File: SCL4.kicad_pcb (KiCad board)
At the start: 2 copper layers, 150.5 x 233.3 mm, 38 parts, among them J1 spare1, J2 spare2, J3 Siemens_A1010-A263, J4 SP1, J5 SP2, J6 Conn_01x08, J7 5V out, U1 MC3487DX, U2 MC3487DX, U3 TRAM Size 2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

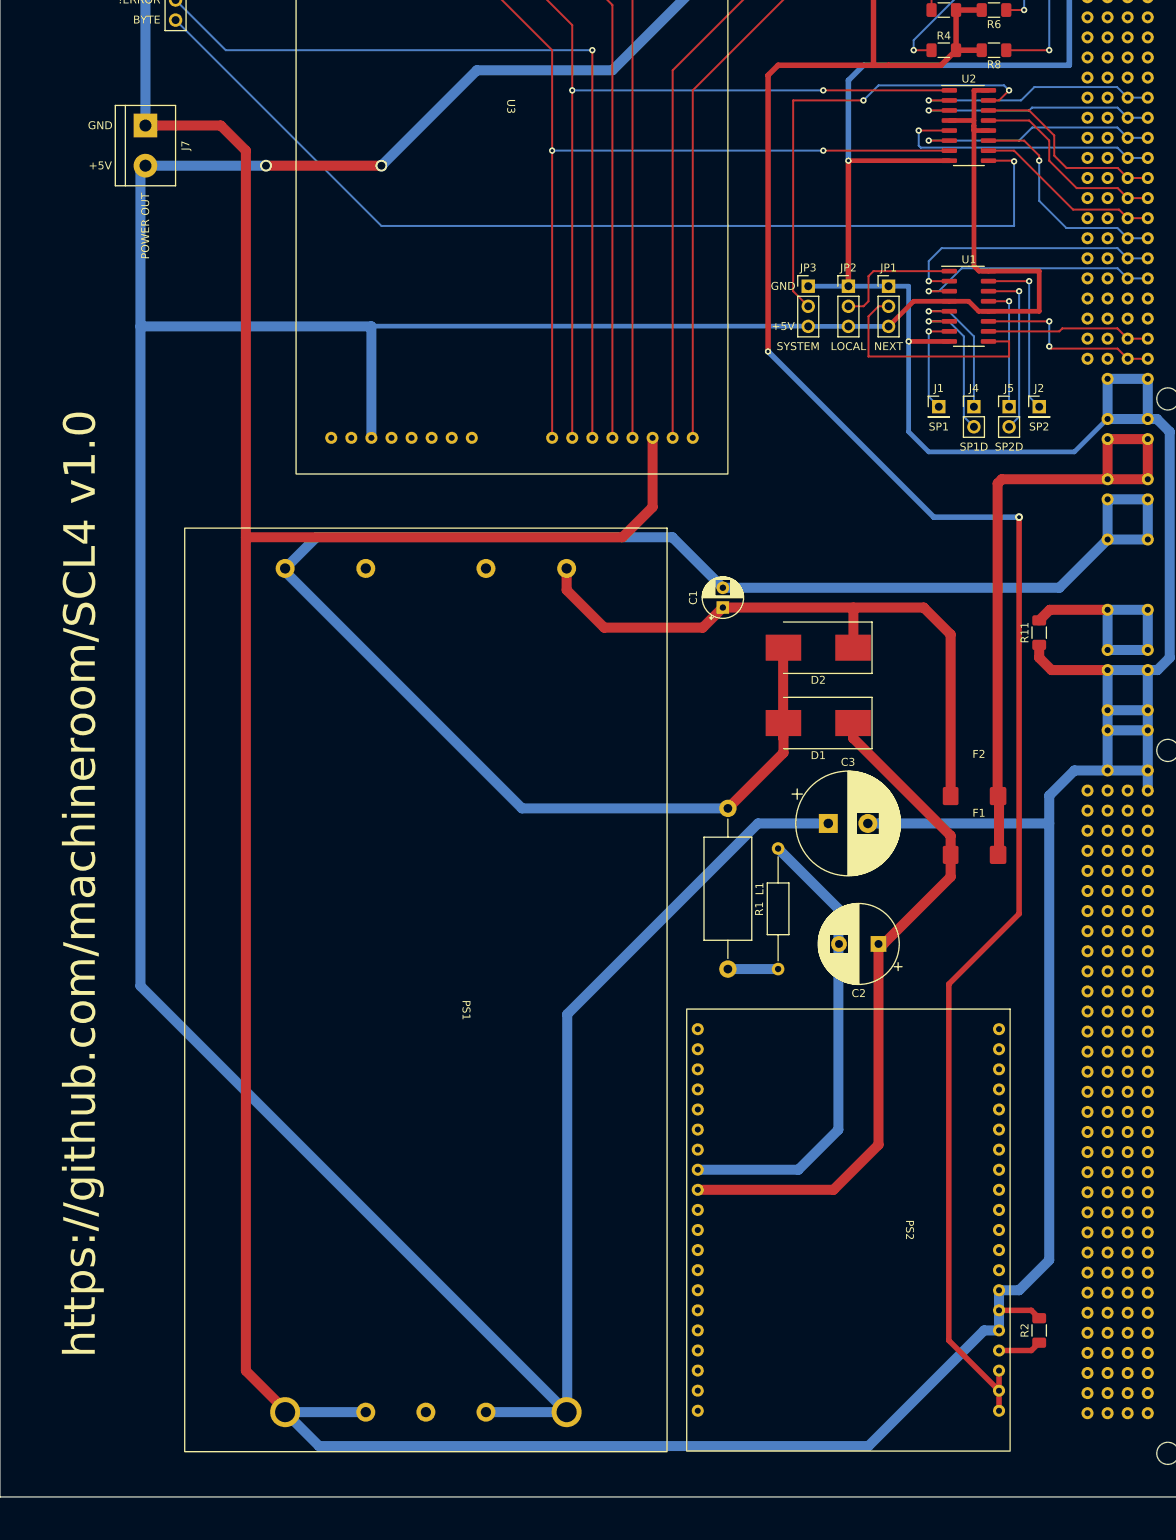
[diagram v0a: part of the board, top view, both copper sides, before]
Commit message: Add HLAA enable jumper
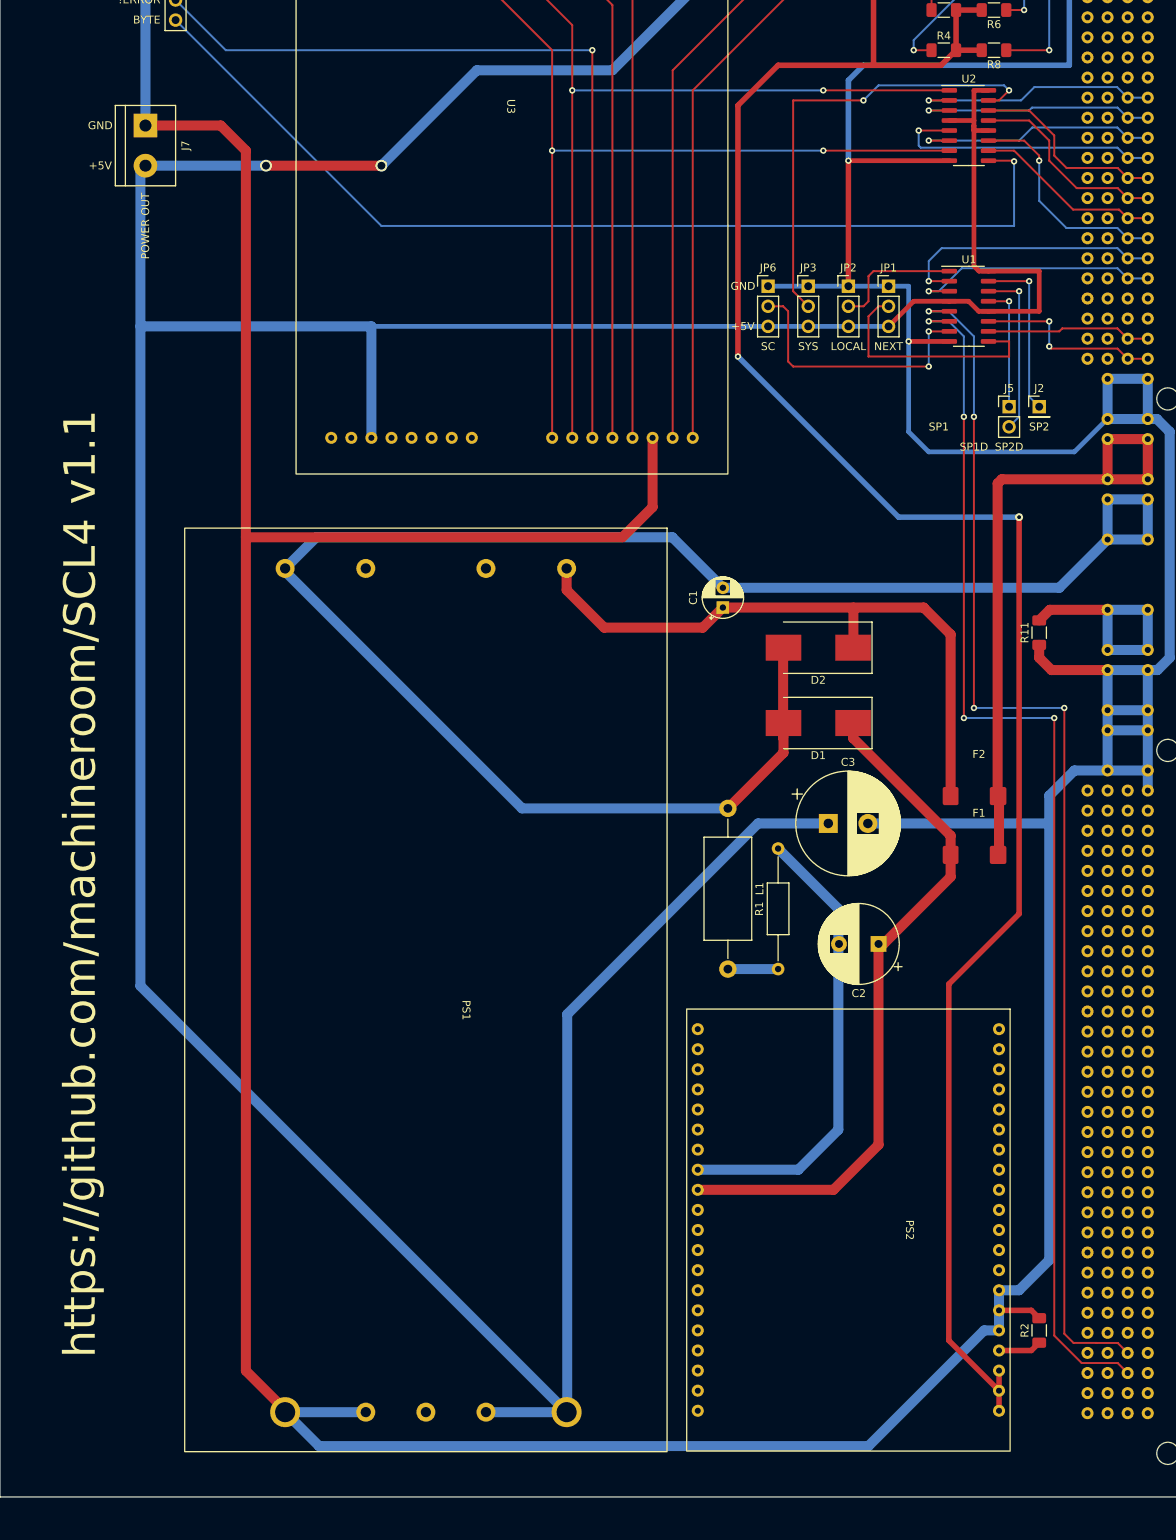
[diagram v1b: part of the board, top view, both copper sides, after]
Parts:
- removed J1: spare1, Connector_PinHeader_2.54mm:PinHeader_1x01_P2.54mm_Vertical
- removed J4: SP1, Connector_PinHeader_2.54mm:PinHeader_1x02_P2.54mm_Vertical
- added JP6: SC MODE, Connector_PinHeader_2.54mm:PinHeader_1x03_P2.54mm_Vertical, F.Cu at (251.5, 96.5)
- R4, R6, R7, R8: value 51R -> 510R
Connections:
- J3 pad B82: unconnected-(J3-PadB82) -> /HLAA_ENABLE
- J3 pad B83: unconnected-(J3-PadB83) -> //HLAA_ENABLE
- U1 pad 5: Net-(J4-Pad1) -> /HLAA_ENABLE
- U1 pad 6: Net-(J4-Pad2) -> //HLAA_ENABLE
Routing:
- net //HLAA_ENABLE: track 0.00 -> 156.9 mm, vias 0 -> 4
- net /HLAA_ENABLE: track 0.00 -> 156.2 mm, vias 0 -> 4
- net Net-(JP6-Pad2): track 12.7 -> 34.2 mm, vias 1 -> 2
- net Net-(J4-Pad2): track 19.8 -> 0.00 mm, vias 1 -> 0
- net Net-(J4-Pad1): track 18.5 -> 0.00 mm, vias 1 -> 0
- net -5V: track 296.2 -> 301.9 mm
- net GND: track 915.3 -> 920.3 mm
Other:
- board text added: "SC"
- board text added: "SYS"
- board text added: "https://github.com/machineroom/SCL4 v1.1"
- board text removed: "SYSTEM"
- board text removed: "https://github.com/machineroom/SCL4 v1.0"

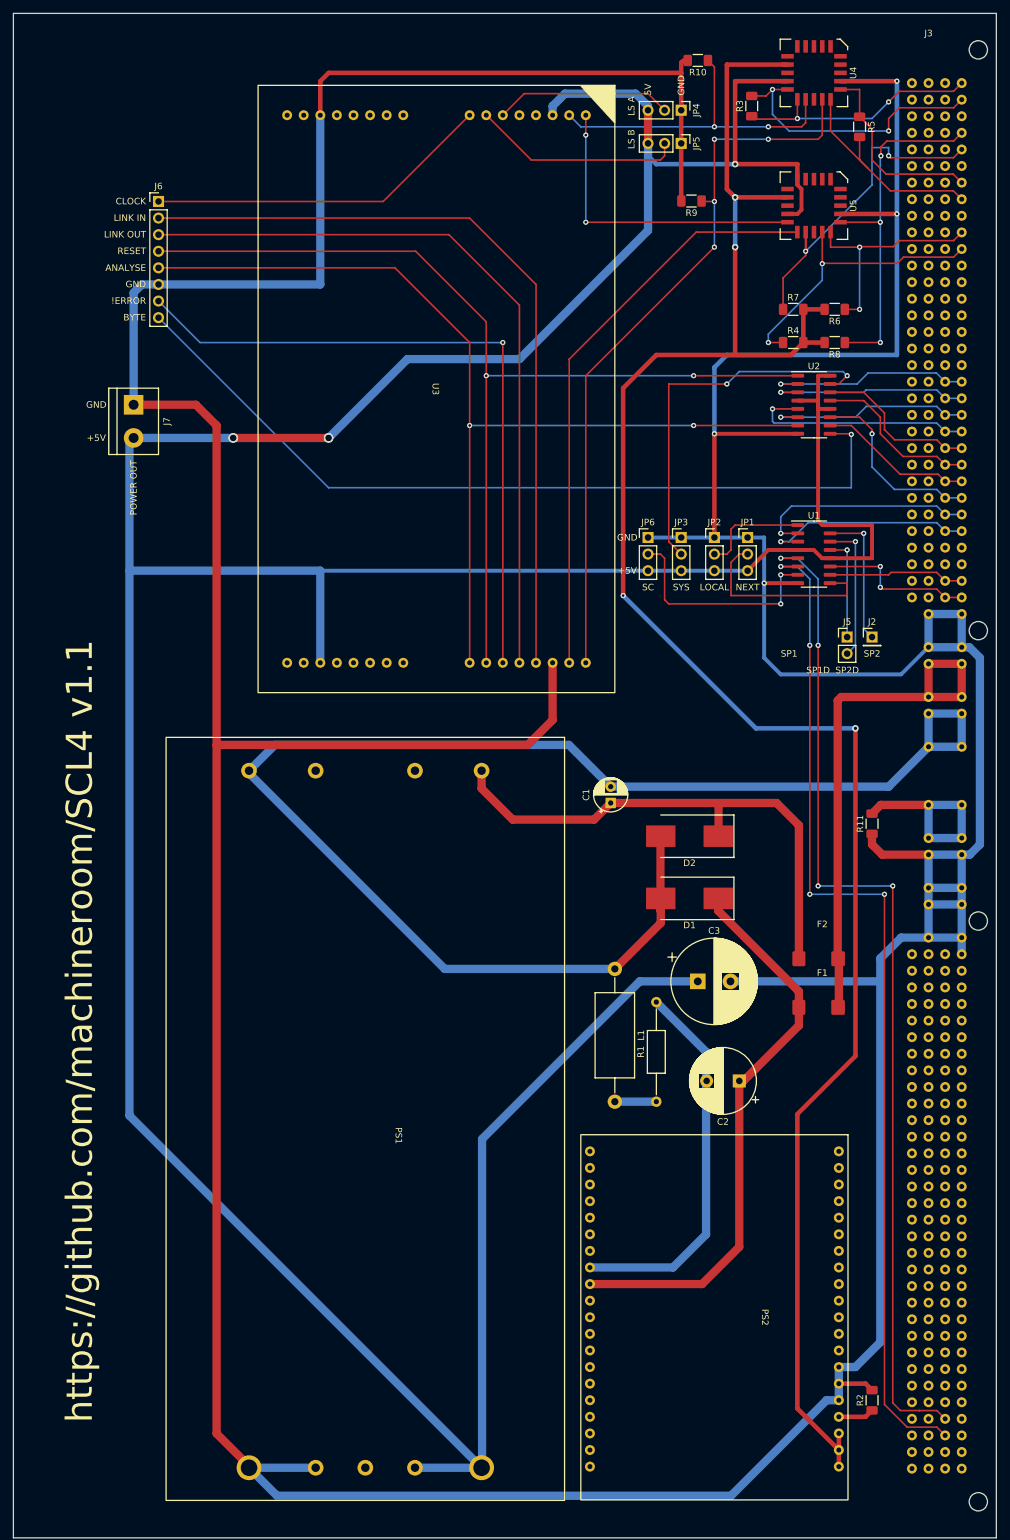
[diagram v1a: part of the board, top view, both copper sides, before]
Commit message: Major rework - fix -5V2 PSU orientation - analyse2 & reset2 signals for proc only operation (no HSL) - bring TRAM L1 and L3 to external header - lay down C3 to reduce height - decoupling - reduce + better match ECL trace lengths - remove R1 - reorder J6 to same as rpi interface header
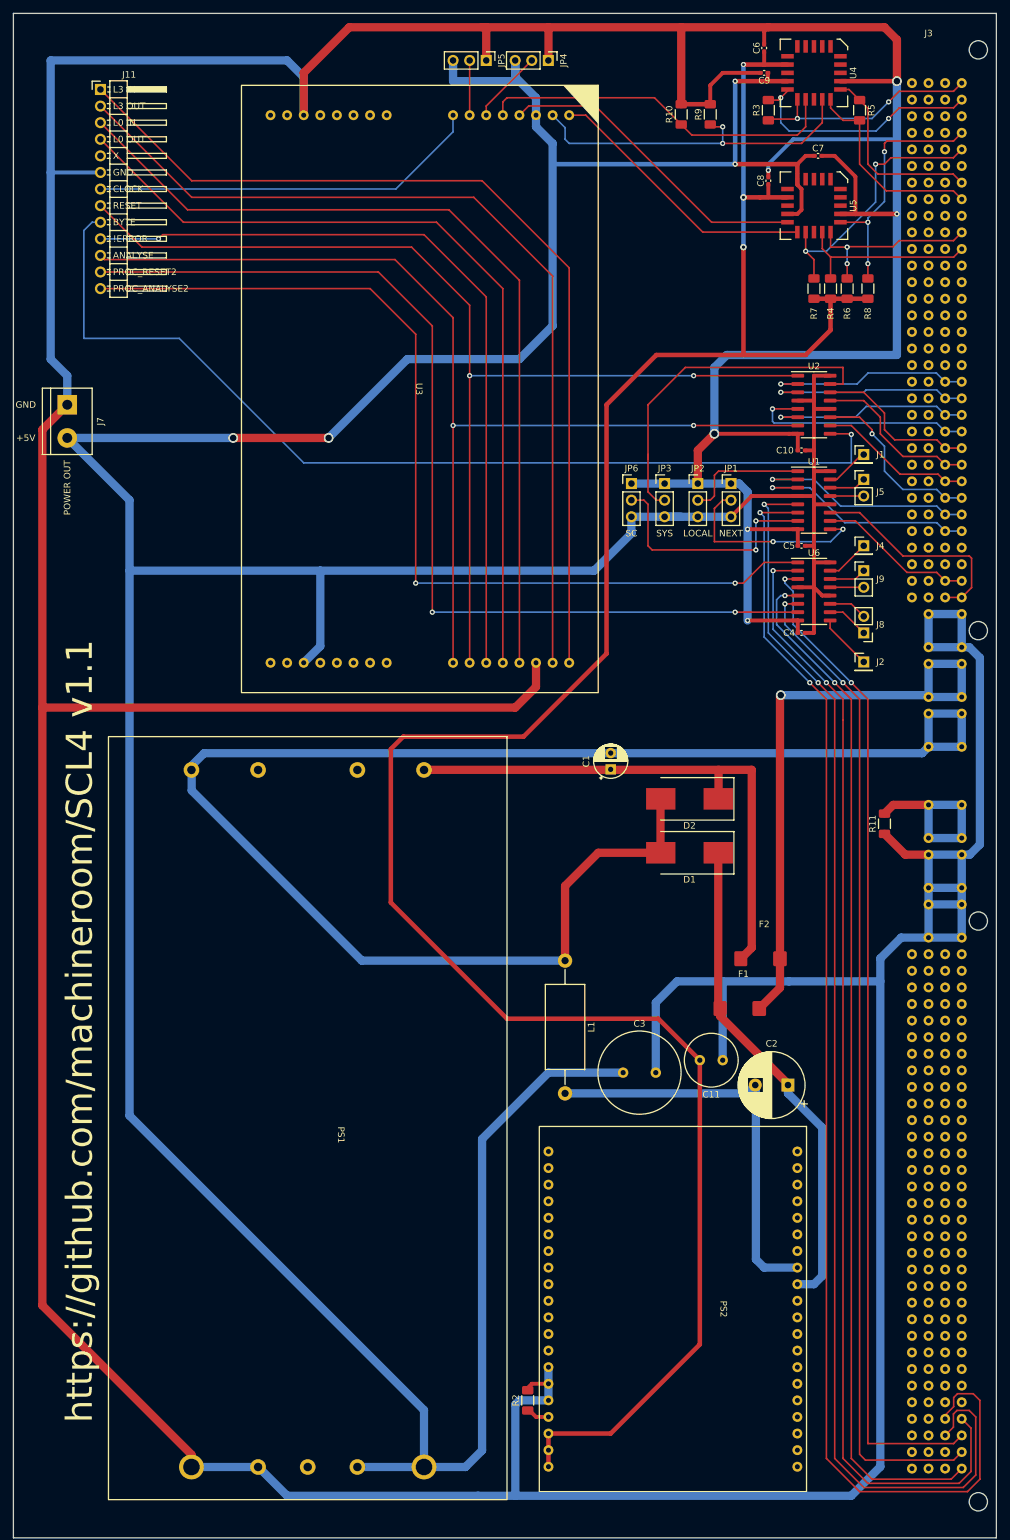
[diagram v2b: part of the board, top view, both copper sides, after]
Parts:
- removed J6: Conn_01x08, Connector_PinHeader_2.54mm:PinHeader_1x08_P2.54mm_Vertical
- removed R1: 10R 2%, Resistor_THT:R_Axial_DIN0207_L6.3mm_D2.5mm_P15.24mm_Horizontal
- added C10: 0.1uF, Capacitor_SMD:C_0402_1005Metric_Pad0.74x0.62mm_HandSolder, F.Cu at (275.0, 83.2)
- added C11: 220uF 63V, Capacitor_THT:C_Radial_D8.0mm_H11.5mm_P3.50mm, F.Cu at (262.9, 176.5)
- added C4: 0.1uF, Capacitor_SMD:C_0402_1005Metric_Pad0.74x0.62mm_HandSolder, F.Cu at (275.0, 111.1)
- added C5: 0.1uF, Capacitor_SMD:C_0402_1005Metric_Pad0.74x0.62mm_HandSolder, F.Cu at (275.0, 97.8)
- added C6: 0.1uF, Capacitor_SMD:C_0402_1005Metric_Pad0.74x0.62mm_HandSolder, F.Cu at (269.2, 21.6)
- added C7: 0.1uF, Capacitor_SMD:C_0402_1005Metric_Pad0.74x0.62mm_HandSolder, F.Cu at (277.5, 38.1)
- added C8: 0.1uF, Capacitor_SMD:C_0402_1005Metric_Pad0.74x0.62mm_HandSolder, F.Cu at (269.9, 41.9)
- added C9: 0.1uF, Capacitor_SMD:C_0402_1005Metric_Pad0.74x0.62mm_HandSolder, F.Cu at (269.2, 25.4)
- added J1: TSPARE1, Connector_PinHeader_2.54mm:PinHeader_1x01_P2.54mm_Vertical, F.Cu at (284.5, 83.8)
- added J11: Conn_01x10_Male, Connector_PinHeader_2.54mm:PinHeader_1x13_P2.54mm_Horizontal, F.Cu at (167.6, 27.9)
- added J4: TSPARE3, Connector_PinHeader_2.54mm:PinHeader_1x01_P2.54mm_Vertical, F.Cu at (284.5, 97.8)
- added J8: SPARE2, Connector_PinHeader_2.54mm:PinHeader_1x02_P2.54mm_Vertical, F.Cu at (284.5, 111.1)
- added J9: SPARE3, Connector_PinHeader_2.54mm:PinHeader_1x02_P2.54mm_Vertical, F.Cu at (284.5, 101.6)
- added U6: MC3487DX, Package_SO:SOIC-16_3.9x9.9mm_P1.27mm, F.Cu at (276.9, 104.8)
- C3: footprint Capacitor_THT:CP_Radial_D13.0mm_P5.00mm -> Capacitor_THT:C_Radial_D12.5mm_H20.0mm_P5.00mm
- J2: value spare2 -> TSPARE2
- J5: value SP2 -> SPARE1
- moved R2 52.7 mm to (233.0, 228.6)
- moved JP5 32.4 mm to (226.7, 23.5)
- moved J5 24.3 mm to (284.5, 87.6)
- moved JP4 21.7 mm to (236.2, 23.5)
- moved C3 18.1 mm to (247.7, 178.4)
- moved R9 13.6 mm to (261.0, 31.8), turned to 90 degrees
- moved F1 12.1 mm to (261.0, 166.4)
- moved J7 10.2 mm to (162.6, 76.2)
- moved R4 10.0 mm to (279.4, 58.4), turned to -90 degrees
- moved R8 9.69 mm to (285.1, 58.4), turned to -90 degrees
- moved F2 8.89 mm to (264.2, 158.8)
- moved PS1 8.82 mm to (229.9, 127.0)
- moved JP2 8.64 mm to (259.1, 88.3)
- moved JP3 8.64 mm to (254.0, 88.3)
- moved JP6 8.64 mm to (248.9, 88.3)
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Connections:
- net /SpeedA renamed Net-(JP4-Pad2)
- net /SpeedB renamed Net-(JP5-Pad2)
- J2 pad 1: Net-(J2-Pad1) -> /TSPARE2
- J3 pad A1: /L2IN -> /L1IN
- J3 pad A10: /L3OUT -> /L2OUT
- J3 pad A11: //L3OUT -> //L2OUT
- J3 pad A2: //L2IN -> //L1IN
- J3 pad A4: /L2OUT -> /L1OUT
- J3 pad A5: //L2OUT -> //L1OUT
- J3 pad A54: GND -> unconnected-(J3-PadA54)
- J3 pad A7: /L3IN -> /L2IN
- J3 pad A8: //L3IN -> //L2IN
- J3 pad A82: unconnected-(J3-PadA82) -> /PROC_ANALYSE2
- J3 pad A83: unconnected-(J3-PadA83) -> //PROC_ANALYSE2
- J3 pad A84: unconnected-(J3-PadA84) -> /PROC_RESET2
- J3 pad A85: unconnected-(J3-PadA85) -> //PROC_RESET2
- J5 pad 1: Net-(J5-Pad1) -> /SPARE1
- J5 pad 2: Net-(J5-Pad2) -> //SPARE1
- L1 pad 2: Net-(L1-Pad2) -> Net-(C2-Pad2)
- R10 pad 1: /TL2in -> /TL1in
- R3 pad 1: /L2IN -> /L1IN
- R3 pad 2: //L2IN -> //L1IN
- R4 pad 1: //L3OUT -> //L2OUT
- R5 pad 1: /L3IN -> /L2IN
- R5 pad 2: //L3IN -> //L2IN
- R6 pad 1: /L3OUT -> /L2OUT
- R7 pad 1: //L2OUT -> //L1OUT
- R8 pad 1: /L2OUT -> /L1OUT
- R9 pad 1: /TL3in -> /TL2in
- U1 pad 13: Net-(J5-Pad1) -> //SPARE1
- U1 pad 14: Net-(J5-Pad2) -> /SPARE1
- U1 pad 15: Net-(J2-Pad1) -> /TSPARE1
- U1 pad 5: /HLAA_ENABLE -> //HLAA_ENABLE
- U1 pad 6: //HLAA_ENABLE -> /HLAA_ENABLE
- U3 pad 31: /TL3out -> /TL3Out
- U3 pad 32: /TL3in -> /TL3In
- U3 pad 4: unconnected-(U3-Pad4) -> /TL1out
- U3 pad 5: unconnected-(U3-Pad5) -> /TL1in
- U4 pad 13: //L2IN -> //L1IN
- U4 pad 14: /L2IN -> /L1IN
- U4 pad 15: /TL2in -> /TL1in
- U4 pad 17: /TL3in -> /TL2in
- U4 pad 18: //L3IN -> //L2IN
- U4 pad 19: /L3IN -> /L2IN
- U5 pad 13: /TL2out -> /TL1out
- U5 pad 14: /TL3out -> /TL2out
- U5 pad 15: //L2OUT -> //L1OUT
- U5 pad 17: //L3OUT -> //L2OUT
- U5 pad 18: /L3OUT -> /L2OUT
- U5 pad 19: /L2OUT -> /L1OUT
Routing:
- net GND: track 920.3 -> 1116.9 mm, vias 4 -> 6
- net /PROC_ANALYSE2: track 0.00 -> 174.7 mm, vias 0 -> 2
- net //PROC_RESET2: track 0.00 -> 158.6 mm, vias 0 -> 2
- net //PROC_ANALYSE2: track 0.00 -> 154.5 mm, vias 0 -> 2
- net /TPROC_RESET2: track 0.00 -> 154.0 mm, vias 0 -> 2
- net /PROC_RESET2: track 0.00 -> 153.4 mm, vias 0 -> 2
- net /TPROC_ANALYSE2: track 0.00 -> 149.1 mm, vias 0 -> 2
- net /TL3In: track 0.00 -> 143.5 mm
- net /TL3Out: track 0.00 -> 139.2 mm
- net /TL3in: track 112.8 -> 0.00 mm, vias 4 -> 0
- net /TL3out: track 89.5 -> 0.00 mm
- net /TL1in: track 0.00 -> 55.7 mm
- net /TL1out: track 0.00 -> 49.0 mm
- net -5V: track 301.9 -> 350.6 mm, vias 4 -> 3
- net /HLAA_ENABLE: track 156.2 -> 201.7 mm, vias 4 -> 2
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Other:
- board text added: "L0 IN"
- board text added: "L0 OUT"
- board text added: "L3 IN"
- board text added: "L3 OUT"
- board text added: "PROC_ANALYSE2"
- board text added: "PROC_RESET2"
- board text added: "X"
- board text removed: "5V"
- board text removed: "LINK IN"
- board text removed: "LINK OUT"
- board text removed: "LS A"
- board text removed: "LS B"
- board text removed: "SP1"
- board text removed: "SP1D"
- board text removed: "SP2"
- board text removed: "SP2D"
